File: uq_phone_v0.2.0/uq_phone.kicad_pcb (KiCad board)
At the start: 4 copper layers, 42.8 x 103.8 mm, 146 parts, among them J1 USB4105-GF-A, J10 SJ-3551B-MSMT-TR-67, J11 Conn_01x02, J2 BM03B-ACHSS-GAN-TF_LF__SN_, J3 20279-001E-03, J4 20279-001E-03, J5 6871XX14022_68715014022, J6 Conn_ARM_SWD_TagConnect_TC2030, J7 Conn_01x02, J8 KP15B-6S-SF_800_, M1 VCDM0834B004L, Q1 MMBT3904LP-7, Q2 MMBT3904LP-7, U1 MCP73871-2CCI_ML, U10 TPD3F303DQDR, U11 TPD8F003DQDR, U12 MCP1664T-E/OT, U13 TS3A5018RSVR, U14 NAU88C22YG, U2 TPS62162DSGR, U3 BQ27441DRZR-G1A, U4 WP SNAP-IN BASE_6000636, U5 TXB0108RGYR, U6 TXB0108RGYR, U7 STM32H733VGTx, U8 LSM6DSVTR, U9 DRV2603RUNR

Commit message: Clean repo
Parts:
- removed J1: USB4105-GF-A, USB_C_connector:GCT_USB4105-GF-A
- removed J10: SJ-3551B-MSMT-TR-67, SJ-3551B-MSMT-TR-67:CUI_SJ-3551B-MSMT-TR-67
- removed J11: Conn_01x02, Connector_Wire:SolderWire-0.25sqmm_1x02_P4.2mm_D0.65mm_OD1.7mm
- removed the J4 at (63.3, 83.3)
- removed the J5 at (31.0, 127.2)
- removed J7: Conn_01x02, Connector_Wire:SolderWire-0.1sqmm_1x02_P3.6mm_D0.4mm_OD1mm
- removed M1: VCDM0834B004L, custom_footprints:Motor_8mm
- removed R30, R31: 22R, Resistor_SMD:R_0402_1005Metric
- removed R34: 3.83R, Resistor_SMD:R_0603_1608Metric
- removed R35, R44, R49: 10k, Resistor_SMD:R_0402_1005Metric
- removed R37, R41, R43, R46, R47: 0R, Resistor_SMD:R_0603_1608Metric
- removed R4: 100k, Resistor_SMD:R_0402_1005Metric
- removed R45: 47k, Resistor_SMD:R_0402_1005Metric
- removed TP1: TestPoint, TestPoint:TestPoint_Pad_D1.5mm
- added J4: 20279-001E-03, 20279-001E-03:IPEX_20279-001E-03, F.Cu at (116.3, 24.4)
- added J4: 20279-001E-03, 20279-001E-03:IPEX_20279-001E-03, F.Cu at (114.3, 67.8)
- added J5: 20279-001E-03, 20279-001E-03:IPEX_20279-001E-03, F.Cu at (138.6, 37.2)
- added J5: 20279-001E-03, 20279-001E-03:IPEX_20279-001E-03, F.Cu at (142.3, 79.1)
- added LED1: XL-1010RGBC, custom_footprints:XL-1010RGBC-WS2812B, B.Cu at (62.0, 107.3)
- added LED10: XL-1010RGBC, custom_footprints:XL-1010RGBC-WS2812B, B.Cu at (64.6, 100.4)
- added LED11: XL-1010RGBC, custom_footprints:XL-1010RGBC-WS2812B, B.Cu at (64.6, 98.1)
- added LED12: XL-1010RGBC, custom_footprints:XL-1010RGBC-WS2812B, B.Cu at (64.6, 95.8)
- added LED13: XL-1010RGBC, custom_footprints:XL-1010RGBC-WS2812B, B.Cu at (67.2, 107.3)
- added LED14: XL-1010RGBC, custom_footprints:XL-1010RGBC-WS2812B, B.Cu at (67.2, 105.0)
- added LED15: XL-1010RGBC, custom_footprints:XL-1010RGBC-WS2812B, B.Cu at (67.2, 102.7)
- added LED16: XL-1010RGBC, custom_footprints:XL-1010RGBC-WS2812B, B.Cu at (67.2, 100.4)
- added LED17: XL-1010RGBC, custom_footprints:XL-1010RGBC-WS2812B, B.Cu at (67.2, 98.1)
- added LED2: XL-1010RGBC, custom_footprints:XL-1010RGBC-WS2812B, B.Cu at (62.0, 105.0)
- added LED3: XL-1010RGBC, custom_footprints:XL-1010RGBC-WS2812B, B.Cu at (62.0, 102.7)
- added LED4: XL-1010RGBC, custom_footprints:XL-1010RGBC-WS2812B, B.Cu at (62.0, 100.4)
- added LED5: XL-1010RGBC, custom_footprints:XL-1010RGBC-WS2812B, B.Cu at (62.0, 98.1)
- added LED6: XL-1010RGBC, custom_footprints:XL-1010RGBC-WS2812B, B.Cu at (62.0, 95.8)
- added LED7: XL-1010RGBC, custom_footprints:XL-1010RGBC-WS2812B, B.Cu at (64.6, 107.3)
- added LED8: XL-1010RGBC, custom_footprints:XL-1010RGBC-WS2812B, B.Cu at (64.6, 105.0)
- added LED9: XL-1010RGBC, custom_footprints:XL-1010RGBC-WS2812B, B.Cu at (64.6, 102.7)
- added R23: 10k, Resistor_SMD:R_0402_1005Metric, F.Cu at (60.5, 28.1)
- added REF**: HIROSE_KP15B-6S-SF_800_, KP15B-6S-SF_800_:HIROSE_KP15B-6S-SF_800_, F.Cu at (54.4, 51.0)
- added SW1: SKTAAAE010, custom_footprints:SKTAAAE010, B.Cu at (39.5, 107.0)
- added SW10: SKTAAAE010, custom_footprints:SKTAAAE010, B.Cu at (44.1, 107.0)
- added SW11: SKTAAAE010, custom_footprints:SKTAAAE010, B.Cu at (44.1, 103.8)
- added SW12: SKTAAAE010, custom_footprints:SKTAAAE010, B.Cu at (44.1, 100.8)
- added SW13: SKTAAAE010, custom_footprints:SKTAAAE010, B.Cu at (44.1, 97.7)
- added SW14: SKTAAAE010, custom_footprints:SKTAAAE010, B.Cu at (44.1, 94.5)
- added SW15: SKTAAAE010, custom_footprints:SKTAAAE010, B.Cu at (44.1, 91.5)
- added SW16: SKSCLCE010, custom_footprints:SKSCLCE010, B.Cu at (79.3, 41.0)
- added SW17: SKTAAAE010, custom_footprints:SKTAAAE010, B.Cu at (44.1, 88.3)
- added SW18: SKTAAAE010, custom_footprints:SKTAAAE010, B.Cu at (44.1, 85.2)
- added SW19: SKTAAAE010, custom_footprints:SKTAAAE010, B.Cu at (48.9, 107.0)
- added SW2: SKTAAAE010, custom_footprints:SKTAAAE010, B.Cu at (39.5, 103.8)
- added SW20: SKTAAAE010, custom_footprints:SKTAAAE010, B.Cu at (48.9, 103.8)
- added SW21: SKTAAAE010, custom_footprints:SKTAAAE010, B.Cu at (48.9, 100.8)
- added SW22: SKSCLCE010, custom_footprints:SKSCLCE010, B.Cu at (84.0, 41.0)
- added SW23: SKTAAAE010, custom_footprints:SKTAAAE010, B.Cu at (48.9, 97.7)
- added SW24: SKTAAAE010, custom_footprints:SKTAAAE010, B.Cu at (48.9, 94.5)
- added SW25: SKTAAAE010, custom_footprints:SKTAAAE010, B.Cu at (48.9, 91.5)
- added SW26: SKTAAAE010, custom_footprints:SKTAAAE010, B.Cu at (48.9, 88.3)
- added SW27: SKTAAAE010, custom_footprints:SKTAAAE010, B.Cu at (48.9, 85.2)
- added SW28: SKTAAAE010, custom_footprints:SKTAAAE010, B.Cu at (53.5, 107.0)
- added SW29: SKTAAAE010, custom_footprints:SKTAAAE010, B.Cu at (53.5, 103.8)
- added SW3: SKTAAAE010, custom_footprints:SKTAAAE010, B.Cu at (39.5, 100.8)
- added SW30: SKTAAAE010, custom_footprints:SKTAAAE010, B.Cu at (53.5, 100.8)
- added SW31: SKTAAAE010, custom_footprints:SKTAAAE010, B.Cu at (53.5, 97.7)
- added SW32: SKTAAAE010, custom_footprints:SKTAAAE010, B.Cu at (53.5, 94.5)
- added SW33: SKTAAAE010, custom_footprints:SKTAAAE010, B.Cu at (53.5, 91.5)
- added SW34: SKTAAAE010, custom_footprints:SKTAAAE010, B.Cu at (53.5, 88.3)
- added SW35: SKTAAAE010, custom_footprints:SKTAAAE010, B.Cu at (53.5, 85.2)
- added SW36: SKTAAAE010, custom_footprints:SKTAAAE010, B.Cu at (58.2, 107.0)
- added SW37: SKTAAAE010, custom_footprints:SKTAAAE010, B.Cu at (58.2, 103.8)
- added SW38: SKTAAAE010, custom_footprints:SKTAAAE010, B.Cu at (58.2, 100.8)
- added SW39: SKTAAAE010, custom_footprints:SKTAAAE010, B.Cu at (58.2, 97.7)
- added SW4: SKTAAAE010, custom_footprints:SKTAAAE010, B.Cu at (39.5, 97.7)
- added SW40: SKTAAAE010, custom_footprints:SKTAAAE010, B.Cu at (58.2, 94.5)
- added SW41: SKTAAAE010, custom_footprints:SKTAAAE010, B.Cu at (58.2, 91.5)
- added SW5: SKTAAAE010, custom_footprints:SKTAAAE010, B.Cu at (39.5, 94.5)
- added SW6: SKSCLCE010, custom_footprints:SKSCLCE010, B.Cu at (78.7, 34.1)
- added SW7: SKTAAAE010, custom_footprints:SKTAAAE010, B.Cu at (39.5, 91.5)
- added SW8: SKTAAAE010, custom_footprints:SKTAAAE010, B.Cu at (39.5, 88.3)
- added SW9: SKTAAAE010, custom_footprints:SKTAAAE010, B.Cu at (39.5, 85.2)
- C1, C15, C16, C17, C18, C5, C6, L1, MK1, R11, U3: moved to B.Cu
- C14: value 100nF -> 4.7uF; moved to B.Cu
- C19: value 4.7uF -> 100nF; moved to B.Cu
- C2: value 4.7uF -> 22uF; footprint Capacitor_SMD:C_0402_1005Metric -> Capacitor_SMD:C_0603_1608Metric; moved to B.Cu
- C20: value 2.2uF -> 100nF; moved to B.Cu
- C21: value 2.2uF -> 100nF
- C25, C26: value 100nF -> 2.2uF
- C27: value 100nF -> 10uF; footprint Capacitor_SMD:C_0402_1005Metric -> Capacitor_SMD:C_0603_1608Metric
- C28, C36: value 100nF -> 4.7uF
- C3: value 4.7uF -> 10uF; footprint Capacitor_SMD:C_0402_1005Metric -> Capacitor_SMD:C_0603_1608Metric; moved to B.Cu
- C34: value 10uF -> 100nF; footprint Capacitor_SMD:C_0603_1608Metric -> Capacitor_SMD:C_0402_1005Metric
- C35: value 4.7uF -> 100nF
- C38: value 1uF -> 100nF
- C39, C41, C43: value 1uF -> 4.7uF
- C4: value 10uF -> 4.7uF; footprint Capacitor_SMD:C_0603_1608Metric -> Capacitor_SMD:C_0402_1005Metric; moved to B.Cu
- C40: value 33pF -> 4.7uF
- C45, C47, C48, C49: value 4.7uF -> 1uF
- C46: value 4.7uF -> 33pF
- C7: value 22uF -> 4.7uF; footprint Capacitor_SMD:C_0603_1608Metric -> Capacitor_SMD:C_0402_1005Metric; moved to B.Cu
- J2: value BM03B-ACHSS-GAN-TF_LF__SN_ -> 124018312112A; footprint BM03B-ACHSS-GAN-TF_LF__SN_:JST_BM03B-ACHSS-GAN-TF_LF__SN_ -> 124018312112A:AMPHENOL_124018312112A
- J3: value 20279-001E-03 -> BM03B-ACHSS-GAN-TF_LF__SN_; footprint 20279-001E-03:IPEX_20279-001E-03 -> BM03B-ACHSS-GAN-TF_LF__SN_:JST_BM03B-ACHSS-GAN-TF_LF__SN_
- J8: value KP15B-6S-SF_800_ -> MCS-302S-C1; footprint KP15B-6S-SF_800_:HIROSE_KP15B-6S-SF_800_ -> custom_footprints:SIM-SMD_MCS-302S-C1
- R1: value 270k -> 100k; moved to B.Cu
- R10: value 0R -> 2.2k; footprint Resistor_SMD:R_0805_2012Metric -> Resistor_SMD:R_0402_1005Metric; moved to B.Cu
- R12: value 4.7k -> 0R
- R13: value 47k -> 0R
- R14, R15: footprint Resistor_SMD:R_0603_1608Metric -> Resistor_SMD:R_0402_1005Metric
- R16, R21, R22: value 0R -> 4.7k; footprint Resistor_SMD:R_0603_1608Metric -> Resistor_SMD:R_0402_1005Metric
- R19: value 0R -> 47k; footprint Resistor_SMD:R_0603_1608Metric -> Resistor_SMD:R_0402_1005Metric
- R2: value 100k -> 5.1k
- R20, R40: value 0R -> 10k; footprint Resistor_SMD:R_0603_1608Metric -> Resistor_SMD:R_0402_1005Metric
- R24, R25: value 4.7k -> 10k
- R26, R27: value 10k -> 22R
- R28: value 0R -> 22R; footprint Resistor_SMD:R_0603_1608Metric -> Resistor_SMD:R_0402_1005Metric
- R29: value 0R -> 3.83R
- R3: value 2.2k -> 5.1k
- R32: value 22R -> 10k
- R36: value 10k -> 2.2k
- R38: value 2.2k -> 47k
- R42: value 0R -> 330R; footprint Resistor_SMD:R_0603_1608Metric -> Resistor_SMD:R_0402_1005Metric; moved to B.Cu
- R5: value 5.1k -> 270k; moved to B.Cu
- R7: value 10k -> 100k; moved to B.Cu
- R8: value 10m -> 10k; footprint Resistor_SMD:R_0805_2012Metric -> Resistor_SMD:R_0402_1005Metric; moved to B.Cu
- R9: value 5.1k -> 10m; footprint Resistor_SMD:R_0402_1005Metric -> Resistor_SMD:R_0805_2012Metric; moved to B.Cu
- TP2, TP3, TP4, TP5, TP6, TP7: moved to F.Cu
- U1: value MCP73871-2CCI_ML -> TPS62162DSGR; footprint MCP73871-2CCI_ML:QFN50P400X400X100-21N -> TPS62162DSGR:SON50P200X200X80-9N; moved to B.Cu
- U10: value TPD3F303DQDR -> TPD8F003DQDR; footprint TPD3F303DQDR:SON40P170X135X80-9N -> TPD8F003DQDR:SON40P135X330X80-17N
- U11: value TPD8F003DQDR -> LSM6DSVTR; footprint TPD8F003DQDR:SON40P135X330X80-17N -> LSM6DSVTR:LGA14-L_2P59X3P1X0P5_STM
- U12: value MCP1664T-E/OT -> DRV2603RUNR; footprint MCP1664T_E_OT:SOT-23-5_OT_MCH -> DRV2603RUNR:QFN50P200X200X80-10N; moved to B.Cu
- U2: value TPS62162DSGR -> MCP73871-2CCI_ML; footprint TPS62162DSGR:SON50P200X200X80-9N -> MCP73871-2CCI_ML:QFN50P400X400X100-21N; moved to B.Cu
- U4: footprint WP_SNAP-IN_BASE:SIERRA_WP_SNAP-IN_BASE -> RC7620_1104625:XCVR_RC7620_1104625
- U6: value TXB0108RGYR -> STM32H733VGHx; footprint TXB0108RGYR:IC_TXB0108RGYR -> Package_BGA:TFBGA-100_8x8mm_Layout10x10_P0.8mm
- U7: value STM32H733VGTx -> TXB0108RGYR; footprint Package_QFP:LQFP-100_14x14mm_P0.5mm -> TXB0108RGYR:IC_TXB0108RGYR
- U8: value LSM6DSVTR -> TPD3F303DQDR; footprint LSM6DSVTR:LGA14-L_2P59X3P1X0P5_STM -> TPD3F303DQDR:SON40P170X135X80-9N
- U9: value DRV2603RUNR -> MCP1664T-E/OT; footprint DRV2603RUNR:QFN50P200X200X80-10N -> MCP1664T_E_OT:SOT-23-5_OT_MCH
- moved R6 138.0 mm to (64.0, 25.0), turned to 180 degrees
- moved C34 126.0 mm to (68.3, 21.9), turned to -90 degrees
- moved R25 126.0 mm to (59.5, 20.2), turned to 0 degrees
- moved C35 125.5 mm to (65.4, 22.6), turned to 0 degrees
- moved R24 117.0 mm to (60.5, 29.1), turned to 180 degrees
- moved C39 116.6 mm to (142.2, 86.0), turned to 0 degrees
- moved C19 116.2 mm to (68.2, 28.9)
- moved C25 115.0 mm to (60.6, 31.1), turned to 180 degrees
- moved R27 114.7 mm to (49.2, 38.7), turned to 0 degrees
- moved R28 113.8 mm to (49.2, 39.6)
- moved C26 112.7 mm to (60.6, 30.2), turned to 180 degrees
- moved R26 112.7 mm to (49.2, 40.6), turned to 0 degrees
- moved U9 108.2 mm to (36.8, 44.0)
- moved R29 107.8 mm to (33.7, 46.2), turned to 0 degrees
- moved L2 107.7 mm to (36.8, 40.1)
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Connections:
- C1 pad 1: VUSB -> GND
- C1 pad 2: GND -> MCP_OUT
- C10 pad 1: +VMOB -> VBAT
- C11 pad 1: +VMOB -> VBAT
- C12 pad 1: +VMOB -> VBAT
- C13 pad 1: +VMOB -> VBAT
- C14 pad 1: +1.8V -> +3.3V
- C15 pad 1: +1.8V -> GND
- C15 pad 2: GND -> +3.3V
- C16 pad 1: +3.3V -> GND
- C16 pad 2: GND -> +3.3V
- C17 pad 1: +3.3V -> GND
- C17 pad 2: GND -> +3.3V
- C18 pad 2: RST -> +3.3V
- C19 pad 1: +3.3V -> GND
- C19 pad 2: GND -> +3.3V
- C2 pad 1: VBAT -> +3.3V
- C20 pad 1: Net-(C20-Pad1) -> GND
- C20 pad 2: GND -> RST
- C21 pad 1: Net-(C21-Pad1) -> +1.8V
- C22 pad 1: GND -> +3.3V
- C22 pad 2: +3.3V -> GND
- C23 pad 1: GND -> +1.8V
- C23 pad 2: +3.3V -> GND
- C24 pad 1: GND -> +3.3V
- C24 pad 2: +3.3V -> GND
- C25 pad 1: GND -> Net-(C25-Pad1)
- C25 pad 2: +3.3V -> GND
- C26 pad 1: GND -> Net-(C26-Pad1)
- C26 pad 2: +3.3V -> GND
- C28 pad 1: +3.3V -> DISP_LEDA
- C3 pad 1: MCP_OUT -> VUSB
- C35 pad 1: DISP_LEDA -> +3.3V
- C36 pad 1: +1.8V -> Net-(MK1-OUTPUT)
- C36 pad 2: GND -> MIC_OUT
- C37 pad 1: HP_MIC -> AGND
- C37 pad 2: Net-(C37-Pad2) -> MIC_GND
- C38 pad 1: HP_LEFT -> +1.8V
- C38 pad 2: Net-(C38-Pad2) -> GND
- C39 pad 1: HP_RIGHT -> Net-(U14-VDDA)
- C39 pad 2: Net-(C39-Pad2) -> AGND
- C4 pad 1: GND -> MCP_OUT
- C4 pad 2: MCP_OUT -> GND
- C40 pad 1: Net-(U14-MCLK) -> Net-(U14-VDDA)
- C40 pad 2: GND -> AGND
- C41 pad 1: Net-(U14-RMICN) -> +1.8V
- C41 pad 2: AGND -> GND
- C42 pad 1: Net-(MK1-OUTPUT) -> +1.8V
- C42 pad 2: MIC_OUT -> GND
- C43 pad 1: AGND -> Net-(U14-VREF)
- C43 pad 2: MIC_GND -> AGND
- C44 pad 1: Net-(U14-VDDB) -> MIC_BIAS
- C44 pad 2: GND -> AGND
- C45 pad 1: MIC_BIAS -> Net-(U14-RMICN)
- C46 pad 1: Net-(U14-VDDB) -> MOB_SYS_CLK
- C47 pad 1: Net-(U14-VDDA) -> Net-(U14-RMICP)
- C47 pad 2: AGND -> HP_MIC
- C48 pad 1: Net-(U14-VREF) -> HP_LEFT
- C48 pad 2: AGND -> Net-(C48-Pad2)
- C49 pad 1: Net-(U14-VDDA) -> HP_RIGHT
- C49 pad 2: AGND -> Net-(C49-Pad2)
- C7 pad 1: +3.3V -> VBAT
- C8 pad 1: +VMOB -> VBAT
- C9 pad 1: +VMOB -> VBAT
- FB1 pad 1: GND -> Net-(U14-VDDA)
- FB1 pad 2: AGND -> +3.3V
- FB2 pad 1: Net-(U14-VDDA) -> GND
- FB2 pad 2: +3.3V -> AGND
- J3 pad 1: MOB_MAIN_ANT -> GND
- J3 pad 2: GND -> BAT_THERM
- J3 pad 3: (no net) -> Net-(U3-BAT)
- L1 pad 1: Net-(U2-SW) -> Net-(U1-SW)
- R1 pad 1: Net-(U1-VPCC) -> Net-(U1-PG)
- R1 pad 2: VUSB -> +3.3V
- R10 pad 1: +VMOB -> Net-(U2-PROG1)
- R10 pad 2: VBAT -> GND
- R11 pad 1: Net-(U2-PG) -> GND
- R11 pad 2: +3.3V -> Net-(U2-PROG3)
- R12 pad 1: Net-(Q1-Pad1) -> Net-(U4A-UART1_TX)
- R12 pad 2: MOB_PWR_CTL -> MOB_TXD
- R13 pad 1: GND -> Net-(U4A-UART1_RTS)
- R13 pad 2: Net-(Q1-Pad1) -> MOB_RTS
- R14 pad 1: /Mobile/MOB_USB_N -> Net-(U4A-UART1_RX)
- R14 pad 2: USB_N -> MOB_RXD
- R15 pad 1: /Mobile/MOB_USB_P -> Net-(U4A-UART1_CTS)
- R15 pad 2: USB_P -> MOB_CTS
- R16 pad 1: Net-(U4A-USB_VBUS) -> Net-(Q1-Pad1)
- R16 pad 2: VUSB -> MOB_PWR_CTL
- R18 pad 2: Net-(Q2-Pad1) -> Net-(Q1-Pad1)
- R19 pad 1: Net-(U4A-UART1_TX) -> GND
- R19 pad 2: MOB_TXD -> Net-(Q2-Pad1)
- R2 pad 2: Net-(U1-VPCC) -> Net-(J2-CC1)
- R20 pad 1: Net-(U4A-UART1_RTS) -> GND
- R20 pad 2: MOB_RTS -> Net-(U6-BOOT0)
- R21 pad 1: Net-(U4A-UART1_RX) -> SCL
- R21 pad 2: MOB_RXD -> +3.3V
- R22 pad 1: Net-(U4A-UART1_CTS) -> SDA
- R22 pad 2: MOB_CTS -> +3.3V
- R24 pad 1: SCL -> MCP_STAT1
- R25 pad 1: SDA -> uSD_DET
- R26 pad 1: MCP_STAT2 -> Net-(U8-DATA2_IN)
- R26 pad 2: +3.3V -> SIM_DATA
- R27 pad 1: MCP_STAT1 -> Net-(U8-DATA1_IN)
- R27 pad 2: +3.3V -> SIM_RST
- R28 pad 1: Net-(U9-LRA/~{ERM}) -> Net-(U8-CLK_IN)
- R28 pad 2: +3.3V -> SIM_CLK
- R29 pad 2: Net-(U9-LRA/~{ERM}) -> DISP_LEDK
- R3 pad 1: Net-(U1-PROG1) -> GND
- R3 pad 2: GND -> Net-(J2-CC2)
- R32 pad 1: Net-(U10-CLK_IN) -> AUD_SW_L
- R32 pad 2: SIM_CLK -> +1.8V
- R33 pad 1: uSD_DET -> GND
- R33 pad 2: +3.3V -> Net-(U13-~{EN})
- R36 pad 1: GND -> HP_MIC
- R36 pad 2: Net-(U13-~{EN}) -> MIC_BIAS
- R38 pad 1: Net-(C37-Pad2) -> HP_DET
- R38 pad 2: MIC_BIAS -> +1.8V
- R39 pad 1: Net-(C38-Pad2) -> Net-(C48-Pad2)
- R40 pad 1: MOB_AUD_SYNC -> Net-(C49-Pad2)
- R40 pad 2: AUD_SYNC -> AGND
- R42 pad 1: MOB_AUD_IN -> Net-(LED15-DI)
- R42 pad 2: AUD_IN -> LED_DATA
- R5 pad 1: GND -> Net-(U2-VPCC)
- R5 pad 2: Net-(J1-CC2) -> VUSB
- R6 pad 1: GND -> FUEL_GPO
- R6 pad 2: Net-(J1-CC1) -> +3.3V
- R7 pad 2: Net-(U3-BIN) -> Net-(U2-VPCC)
- R8 pad 1: Net-(U3-BAT) -> GND
- R8 pad 2: VBAT -> Net-(U3-BIN)
- R9 pad 1: FUEL_GPO -> Net-(U3-BAT)
- R9 pad 2: +3.3V -> VBAT
- TP2 pad 1: GND -> VUSB
- TP4 pad 1: AGND -> VBAT
- TP5 pad 1: VBAT -> +1.8V
- TP6 pad 1: +VMOB -> GND
- TP7 pad 1: +1.8V -> AGND
- TP8 pad 1: Net-(U4A-TP1_BOOTPIN) -> Net-(U4A-TX_ON)
- TP9 pad 1: Net-(U4A-TX_ON) -> Net-(U4A-TP1_BOOTPIN)
- U1 pad 1: MCP_OUT -> GND
- U1 pad 2: Net-(U1-VPCC) -> MCP_OUT
- U1 pad 3: VUSB -> MCP_OUT
- U1 pad 4: VUSB -> GND
- U1 pad 5: BAT_THERM -> GND
- U1 pad 6: MCP_PG -> +3.3V
- U1 pad 7: MCP_STAT2 -> Net-(U1-SW)
- U1 pad 8: MCP_STAT1 -> Net-(U1-PG)
- U1 pad 9: VUSB -> GND
- U10 pad 1: Net-(J8B-RST) -> uSD_DAT2
- U10 pad 2: Net-(J8B-CLK_2) -> uSD_DAT3
- U10 pad 3: Net-(J8B-I/O) -> uSD_CMD
- U10 pad 4: (no net) -> uSD_CLK
- U10 pad 5: SIM_VDD -> uSD_DET
- U10 pad 6: Net-(U10-DATA2_IN) -> uSD_DAT0
- U10 pad 7: Net-(U10-CLK_IN) -> uSD_DAT1
- U10 pad 8: Net-(U10-DATA1_IN) -> unconnected-(U10-CH8_IN-Pad8)
- U10 pad 9: GND -> unconnected-(U10-CH8_OUT-Pad9)
- U11 pad 1: uSD_DAT2 -> GND
- U11 pad 10: Net-(J8A-DAT1) -> unconnected-(U11-OCS_AUX-Pad10)
- U11 pad 11: Net-(J8A-DAT0) -> unconnected-(U11-SDO_AUX-Pad11)
- U11 pad 12: Net-(U11-CH5_OUT) -> +3.3V
- U11 pad 13: Net-(J8A-CLK) -> SCL
- U11 pad 14: Net-(J8A-CMD) -> SDA
- U11 pad 2: uSD_DAT3 -> GND
- U11 pad 3: uSD_CMD -> GND
- U11 pad 4: uSD_CLK -> unconnected-(U11-INT1-Pad4)
- U11 pad 5: uSD_DET -> +3.3V
- U11 pad 6: uSD_DAT0 -> GND
- U11 pad 7: uSD_DAT1 -> GND
- U11 pad 8: unconnected-(U11-CH8_IN-Pad8) -> +3.3V
- U12 pad 1: Net-(D2-A) -> VIB_EN
- U12 pad 2: GND -> VIB_PWM
- U12 pad 3: DISP_LEDK -> GND
- U12 pad 4: DISP_BL -> (no net)
- U12 pad 5: +3.3V -> GND
- U14 pad 11: Net-(U14-MCLK) -> MOB_SYS_CLK
- U14 pad 13: Net-(U14-VDDB) -> +1.8V
- U14 pad 14: Net-(U14-VDDB) -> +1.8V
- U14 pad 4: HP_MIC -> Net-(U14-RMICP)
- U2 pad 1: GND -> MCP_OUT
- U2 pad 2: MCP_OUT -> Net-(U2-VPCC)
- U2 pad 3: MCP_OUT -> VUSB
- U2 pad 4: GND -> VUSB
- U2 pad 5: GND -> BAT_THERM
- U2 pad 6: +3.3V -> MCP_PG
- U2 pad 7: Net-(U2-SW) -> MCP_STAT2
- U2 pad 8: Net-(U2-PG) -> MCP_STAT1
- U2 pad 9: GND -> VUSB
- U4 pad 12: /Mobile/MOB_USB_N -> unconnected-(U4A-USB_D--Pad12)
- U4 pad 13: /Mobile/MOB_USB_P -> unconnected-(U4A-USB_D+-Pad13)
- U4 pad 157: +VMOB -> VBAT
- U4 pad 158: +VMOB -> VBAT
- U4 pad 16: Net-(U4A-USB_VBUS) -> unconnected-(U4A-USB_VBUS-Pad16)
- U4 pad 61: +VMOB -> VBAT
- U4 pad 62: +VMOB -> VBAT
- U4 pad 63: +VMOB -> VBAT
- U7 pad 1: PB_HASH -> AUD_SDA
- U7 pad 10: GND -> +1.8V
- U7 pad 11: +3.3V -> GND
- U7 pad 12: PB_8 -> MCU_AUD_OUT_L_H
- U7 pad 13: PB_9 -> MCU_AUD_BCLK_H
- U7 pad 14: RST -> AUD_SW_H
- U7 pad 15: PB_MENU_L -> MCU_AUD_SYNC_H
- U7 pad 16: PB_MENU_R -> HP_DET_MCU
- U7 pad 17: unconnected-(U7-PC2_C-Pad17) -> MOB_WAKE_H
- U7 pad 18: unconnected-(U7-PC3_C-Pad18) -> SCL
- U7 pad 19: GND -> +3.3V
- U7 pad 2: PB_1 -> +1.8V
- U7 pad 20: unconnected-(U7-VREF+-Pad20) -> SDA
- U7 pad 21: unconnected-(U7-VDDA-Pad21) -> GND
- U7 pad 3: PB_2 -> AUD_SCL
- U7 pad 4: PB_3 -> MOB_WAKE_L
- U7 pad 5: PB_4 -> HP_DET
- U7 pad 6: unconnected-(U7-VBAT-Pad6) -> MCU_AUD_SYNC_L
- U7 pad 7: PB_5 -> AUD_SW_L
- U7 pad 8: PB_6 -> MCU_AUD_BCLK_L
- U7 pad 9: PB_7 -> MCU_AUD_OUT_L
- U8 pad 1: GND -> Net-(J8B-SIM_1_RST)
- U8 pad 2: GND -> Net-(J8B-SIM_1_CLK)
- U8 pad 3: GND -> Net-(J8B-SIM_1_DATA)
- U8 pad 4: unconnected-(U8-INT1-Pad4) -> (no net)
- U8 pad 5: +3.3V -> SIM_VDD
- U8 pad 6: GND -> Net-(U8-DATA2_IN)
- U8 pad 7: GND -> Net-(U8-CLK_IN)
- U8 pad 8: +3.3V -> Net-(U8-DATA1_IN)
- U8 pad 9: unconnected-(U8-INT2-Pad9) -> GND
- U9 pad 1: VIB_EN -> Net-(D2-A)
- U9 pad 2: VIB_PWM -> GND
- U9 pad 3: Net-(U9-LRA/~{ERM}) -> DISP_LEDK
- U9 pad 4: (no net) -> DISP_BL
- U9 pad 5: GND -> +3.3V
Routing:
- net +3.3V: track 246.4 -> 0.00 mm, vias 16 -> 0
- net +1.8V: track 115.8 -> 0.00 mm, vias 6 -> 0
- net AGND: track 111.9 -> 0.00 mm, vias 5 -> 0
- net Net-(MK1-OUTPUT): track 109.6 -> 0.00 mm, vias 2 -> 0
- net MIC_BIAS: track 106.3 -> 0.00 mm, vias 3 -> 0
- net SDA: track 91.7 -> 0.00 mm, vias 6 -> 0
- net SCL: track 91.6 -> 0.00 mm, vias 6 -> 0
- net HP_DET: track 89.6 -> 0.00 mm, vias 5 -> 0
- net +VMOB: track 81.8 -> 0.00 mm, vias 3 -> 0
- net GND: track 81.8 -> 0.00 mm, vias 375 -> 148
- net Net-(C37-Pad2): track 81.7 -> 0.00 mm, vias 2 -> 0
- net HP_RIGHT: track 78.2 -> 0.00 mm, vias 2 -> 0
- net HP_LEFT: track 75.5 -> 0.00 mm, vias 2 -> 0
- net Net-(U4A-USB_VBUS): track 63.0 -> 0.00 mm, vias 2 -> 0
- net /Mobile/MOB_USB_N: track 63.0 -> 0.00 mm, vias 2 -> 0
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- added copper zone on In3.Cu, net GND
- added copper zone on In4.Cu, net GND
- removed copper zone on F.Cu, net +VMOB
- removed copper zone on B.Cu, net AGND
- removed copper zone on F.Cu, net AGND
- removed copper zone on F.Cu, net MCP_OUT
- removed copper zone on F.Cu, net Net-(U2-SW)
- removed copper zone on F.Cu, net Net-(U3-BAT)
- removed copper zone on F.Cu, net VBAT
- removed copper zone on F.Cu, net VUSB
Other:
- board size 42.8 x 103.8 mm -> 118.2 x 108 mm
- copper layers 4 -> 6
- board text added: "Battery"
- board text added: "Non Socket Version"
- board text added: "Socket Version"
- board text added: "THIS IS A BACK VIEW R L"
- board text removed: "LEFT"
- board text removed: "RIGHT"

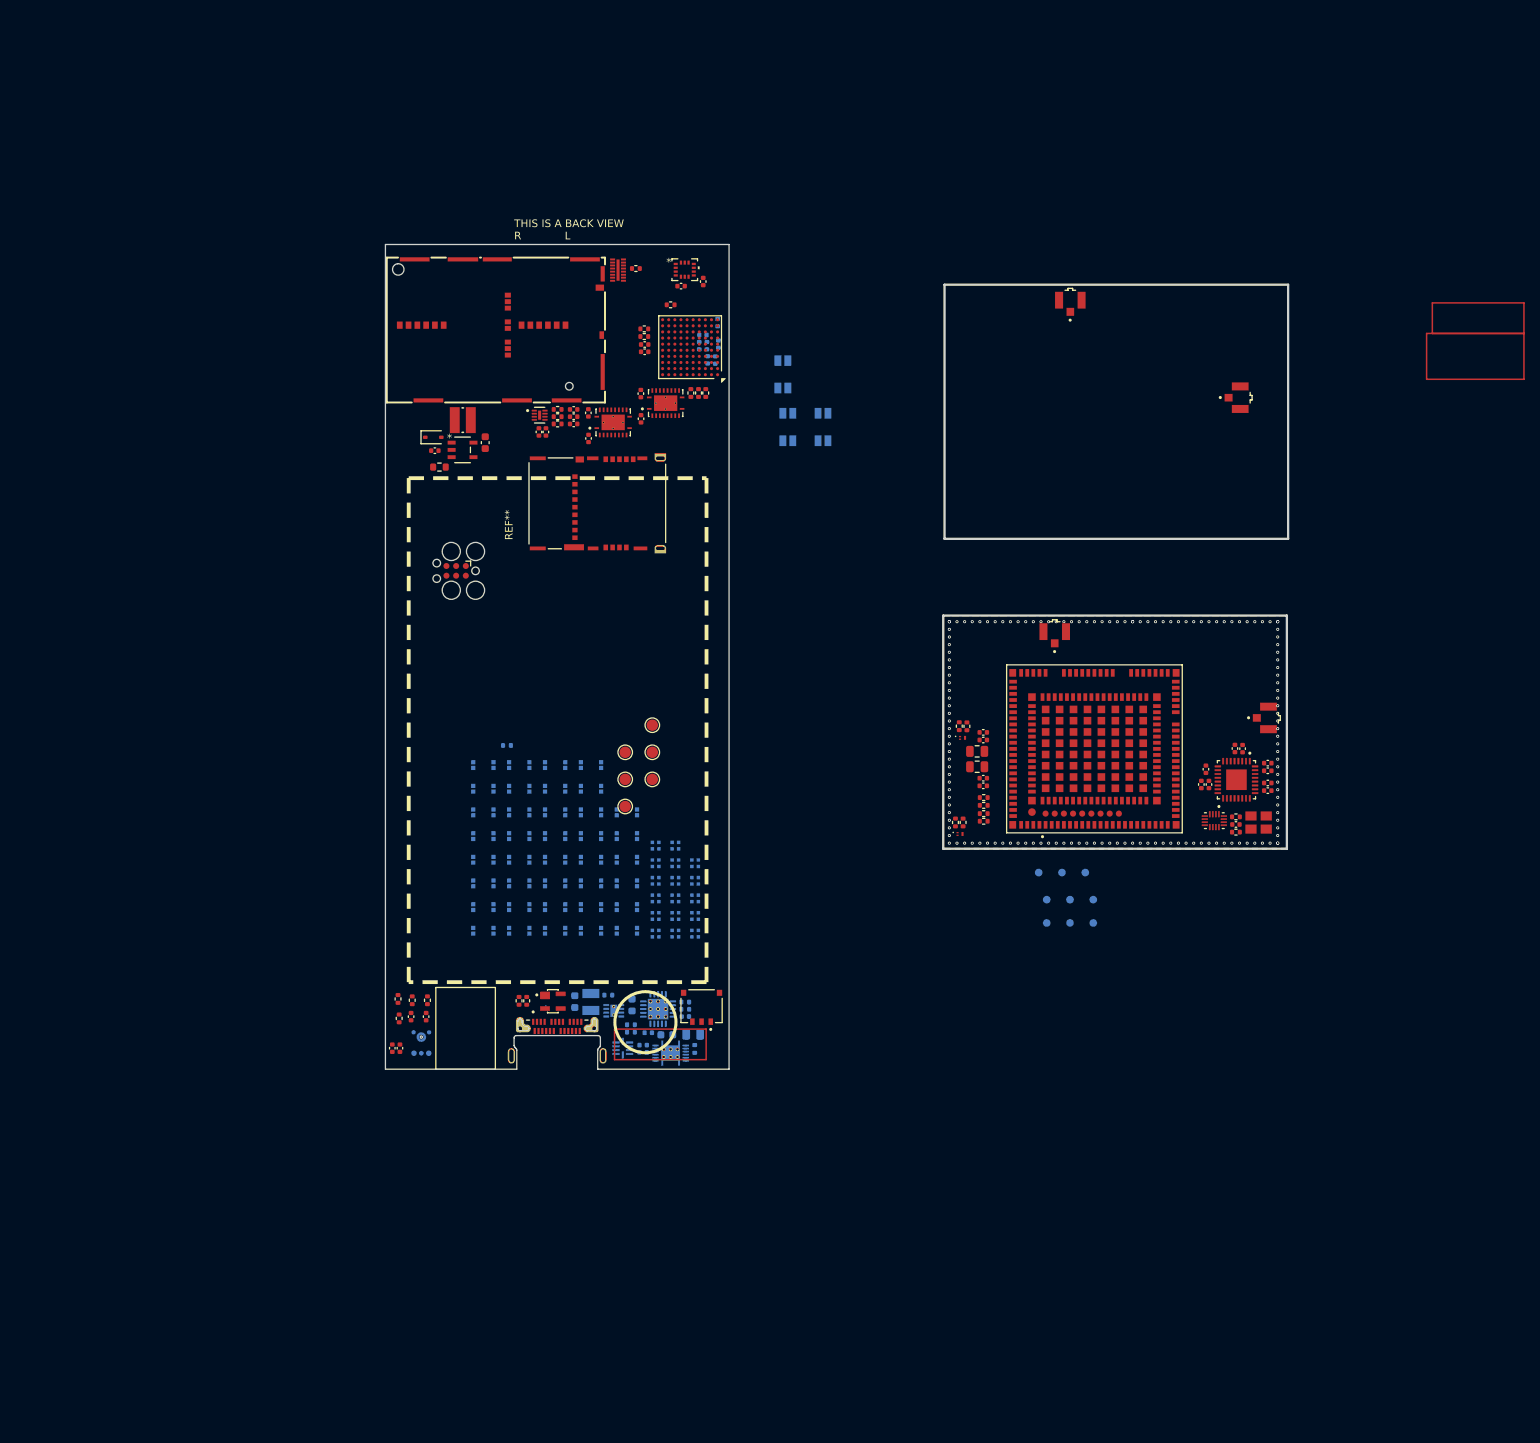
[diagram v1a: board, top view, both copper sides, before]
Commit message: Add more footprints, reduce sizes
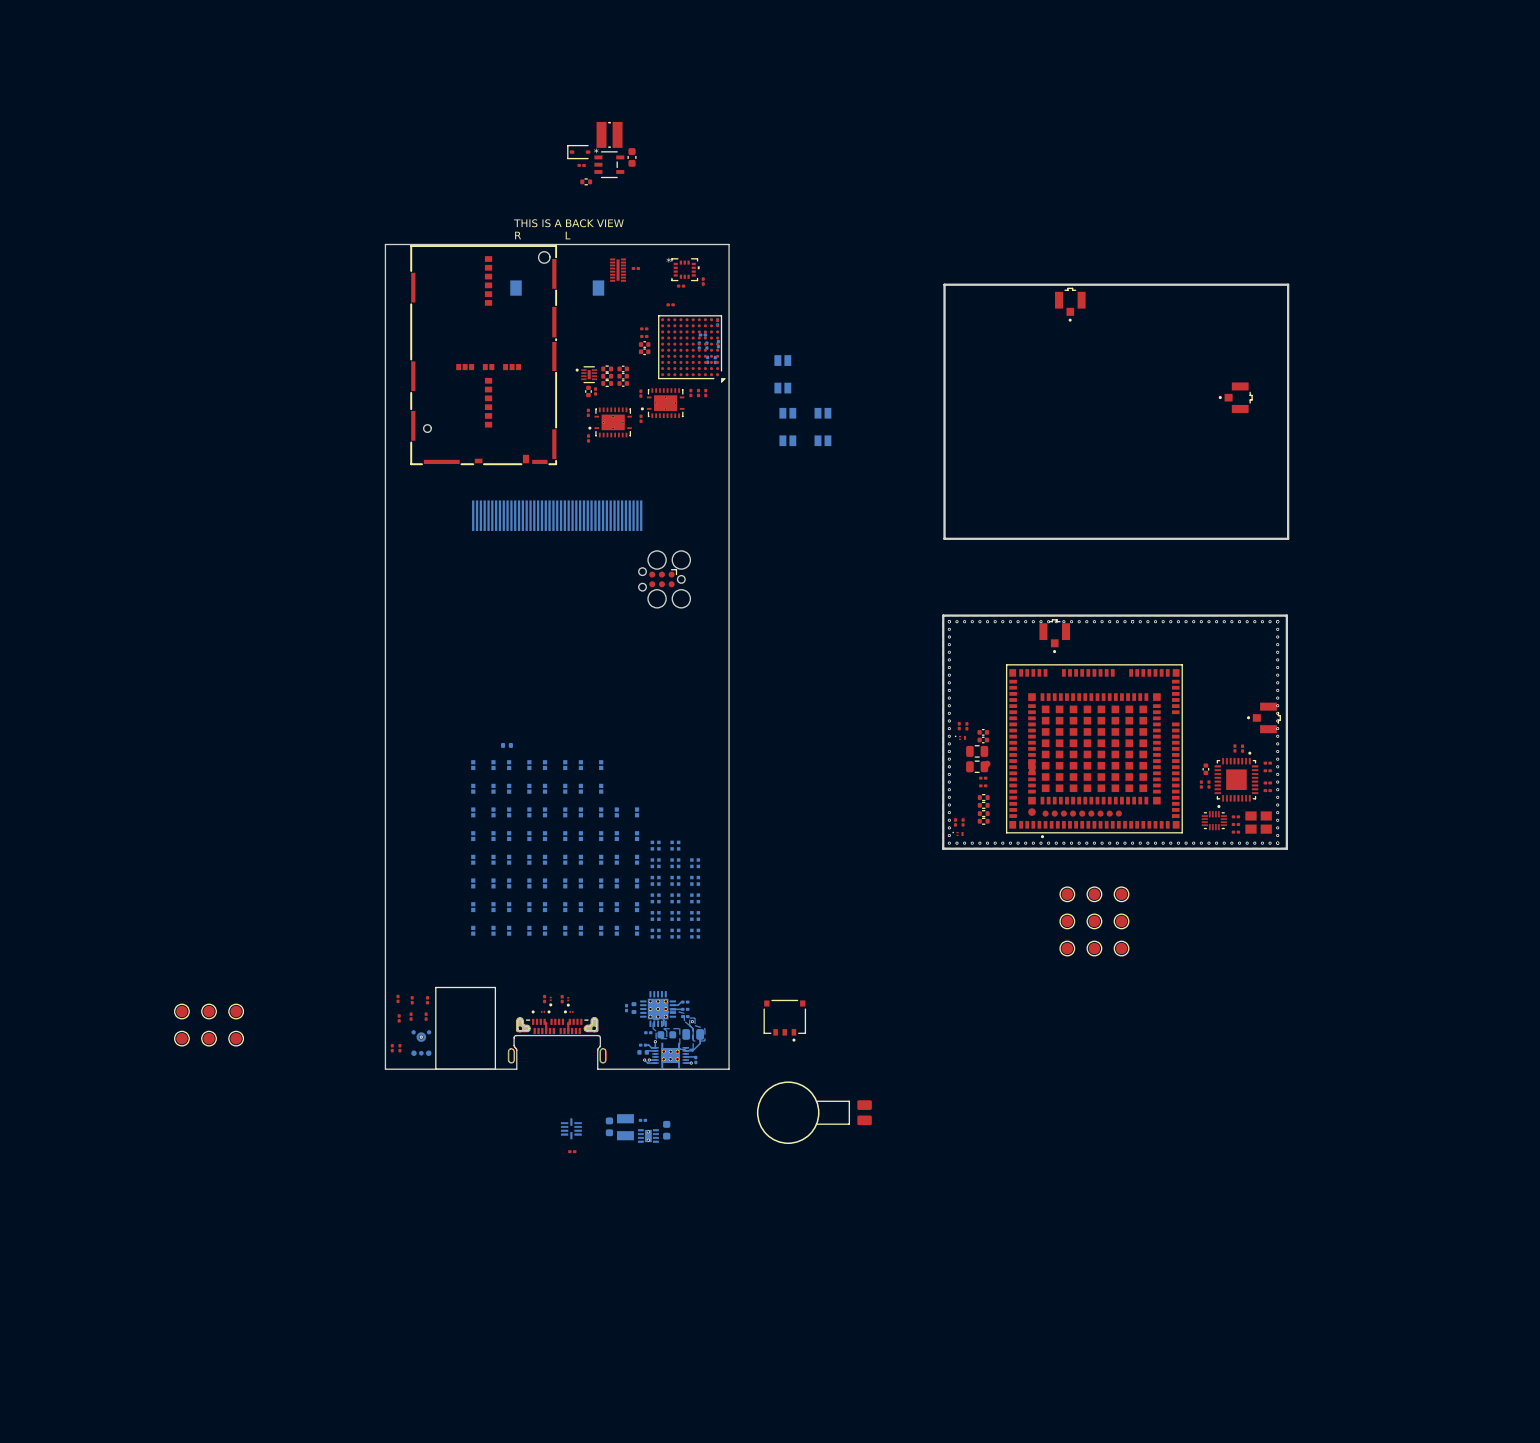
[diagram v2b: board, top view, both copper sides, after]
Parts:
- removed D1: SP0503BAHTG, SP0503BAHTG:SOT143
- removed REF**: HIROSE_KP15B-6S-SF_800_, KP15B-6S-SF_800_:HIROSE_KP15B-6S-SF_800_
- removed TP7: TestPoint, TestPoint:TestPoint_Pad_D1.5mm
- added C29: 100nF, Capacitor_SMD:C_0201_0603Metric, F.Cu at (51.1, 135.9)
- added D4: ESD441DPYR, ESD441DPLR:DIODFN60X30X32-2N, F.Cu at (47.3, 117.6)
- added D5: ESD441DPYR, ESD441DPLR:DIODFN60X30X32-2N, F.Cu at (51.0, 117.6)
- added D6: ESD441DPYR, ESD441DPLR:DIODFN60X30X32-2N, F.Cu at (50.6, 115.9)
- added D7: ESD441DPYR, ESD441DPLR:DIODFN60X30X32-2N, F.Cu at (48.3, 115.9)
- added Disp1: AFR240320A0-2.0INTM, custom_footprints:Display, B.Cu at (49.1, 50.7)
- added M1: C08-00A, custom_footprints:Motor_8mm, F.Cu at (79.4, 130.8)
- added SP1: MCABS-258-RC, custom_footprints:MCABS-258-RC, B.Cu at (49.1, 20.5)
- added TP1: TestPoint, TestPoint:TestPoint_Pad_D1.5mm, F.Cu at (0.00, 117.5)
- C10, C11, C14, C15, C16, C17, C18, C19, C20, C21, C22, C23, C24, C28, C32, C34, C35, C36, C37, C38, C39, C4, C40, C41, C42, C43, C44, C45, C47, C48, C49, C6, C7: footprint Capacitor_SMD:C_0402_1005Metric -> Capacitor_SMD:C_0201_0603Metric
- R1, R10, R11, R16, R17, R18, R19, R2, R20, R21, R22, R23, R24, R25, R3, R32, R33, R36, R38, R39, R40, R6, R7, R8: footprint Resistor_SMD:R_0402_1005Metric -> Resistor_SMD:R_0201_0603Metric
- R29: footprint Resistor_SMD:R_0603_1608Metric -> Resistor_SMD:R_0402_1005Metric
- TP10, TP11, TP12, TP13, TP14, TP15, TP16, TP8, TP9: footprint TestPoint:TestPoint_Pad_D1.0mm -> TestPoint:TestPoint_Pad_D1.5mm; moved to F.Cu
- moved TP4 71.1 mm to (3.55, 121.1), turned to 0 degrees
- moved TP2 70.3 mm to (0.00, 121.1), turned to 0 degrees
- moved TP3 67.2 mm to (3.55, 117.5), turned to 0 degrees
- moved TP6 61.2 mm to (7.10, 121.1), turned to 0 degrees
- moved TP5 57.6 mm to (7.10, 117.5), turned to 0 degrees
- moved C27 42.0 mm to (58.9, 5.70)
- moved C28 42.0 mm to (52.3, 6.75)
- moved R29 42.0 mm to (52.9, 8.90)
- moved D2 42.0 mm to (52.1, 5.00)
- moved L2 42.0 mm to (56.0, 2.75)
- moved U9 42.0 mm to (56.0, 6.65)
- moved J6 27.0 mm to (62.9, 61.0)
- moved C2 17.0 mm to (56.0, 132.7)
- moved R1 17.0 mm to (60.4, 131.8)
- moved L1 17.0 mm to (58.1, 132.7)
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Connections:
- J2 pad A4: Net-(J2-VBUS_A) -> VUSB
- J2 pad A9: Net-(J2-VBUS_A) -> VUSB
- J2 pad B4: Net-(J2-VBUS_B) -> VUSB
- J2 pad B9: Net-(J2-VBUS_B) -> VUSB
- J8 pad 21: unconnected-(J8A-SW/CD-Pad21) -> uSD_SIM_CD
- J8 pad 22: unconnected-(J8A-S/GND-Pad22) -> GND
- J8 pad 23: unconnected-(J8A-GND-Pad23) -> GND
- R25 pad 1: uSD_DET -> uSD_SIM_CD
- TP2 pad 1: VUSB -> +3.3V
- TP3 pad 1: +3.3V -> VBAT
- TP4 pad 1: VBAT -> +1.8V
- TP5 pad 1: +1.8V -> GND
- TP6 pad 1: GND -> AGND
- U12 pad 3: GND -> +3.3V
- U8 pad 6: Net-(U8-DATA2_IN) -> SIM_DATA
- U8 pad 7: Net-(U8-CLK_IN) -> SIM_CLK
- U8 pad 8: Net-(U8-DATA1_IN) -> SIM_RST
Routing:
- net Net-(U3-BAT): track 0.00 -> 11.5 mm, vias 0 -> 2
- net VUSB: track 0.00 -> 2.57 mm
- net VBAT: track 0.00 -> 1.73 mm
- net SDA: track 0.00 -> 1.59 mm, vias 0 -> 1
- net Net-(U3-BIN): track 0.00 -> 1.36 mm
- net Net-(U2-PROG3): track 0.00 -> 1.28 mm
- net Net-(U3-VDD): track 0.00 -> 1.23 mm
- net Net-(U2-PROG1): track 0.00 -> 1.12 mm
- net SCL: track 0.00 -> 0.82 mm, vias 0 -> 1
- net FUEL_GPO: track 0.00 -> 0.73 mm, vias 0 -> 1
- added copper zone on B.Cu, net Net-(U3-BAT)
- added copper zone on B.Cu, net VBAT
- added copper zone on B.Cu, net VUSB
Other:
- board text removed: "Battery"

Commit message: Various Changes to footprints and components
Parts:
- removed the C29 at (57.8, 34.4)
- removed R26, R27, R28: 22R, Resistor_SMD:R_0402_1005Metric
- added TP7: TestPoint, TestPoint:TestPoint_Pad_D1.5mm, F.Cu at (16.3, 108.3)
- added U15: TPS22964CYZPR, TPS22964CYZPR:IC_SN74LVC2G34YZPR, B.Cu at (54.7, 133.2)
- C30: value 22pF -> 1uF; footprint Capacitor_SMD:C_0402_1005Metric -> Capacitor_SMD:C_0201_0603Metric; moved to B.Cu
- C31: value 22pF -> 100nF; footprint Capacitor_SMD:C_0402_1005Metric -> Capacitor_SMD:C_0201_0603Metric; moved to B.Cu
- FB1, FB2: value MPZ2012S221AT000 -> BLM18SG221TN1D; footprint MPZ2012S221AT000:BEADC2012X105N -> BLM18SG221TN1D:BEADC1608X65N
- L2: footprint WE-MAPI_3015:WE-MAPI_3015 -> custom_footprints:IND-SMD_L2.0-W1.2_MTQH201208S4R7MBT
- U12: moved to F.Cu
- U5, U7: value TXB0108RGYR -> TXB0108YZPR2; footprint TXB0108RGYR:IC_TXB0108RGYR -> TXB0108YZPR2:YZP20
- moved C30 100.3 mm to (56.8, 133.7)
- moved C31 99.2 mm to (56.1, 134.5)
- moved FB1 96.5 mm to (58.1, 45.1), turned to 90 degrees
- moved C38 94.6 mm to (56.1, 45.8)
- moved R32 94.6 mm to (56.1, 44.8)
- moved R33 94.6 mm to (56.1, 46.8)
- moved U13 94.6 mm to (53.3, 45.3)
- moved C42 94.5 mm to (52.7, 40.5)
- moved C45 94.4 mm to (56.1, 36.0)
- moved C47 94.4 mm to (57.1, 36.0)
- moved C39 94.4 mm to (60.4, 38.9)
- moved C40 94.4 mm to (60.4, 41.5)
- moved C43 94.4 mm to (60.4, 40.5)
- moved C44 94.4 mm to (60.4, 37.9)
- moved C46 94.4 mm to (52.3, 38.7)
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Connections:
- C27 pad 1: +3.3V -> +3.3V_SW
- C30 pad 1: SIM_RST -> +3.3V
- C31 pad 1: SIM_DATA -> +3.3V_SW
- FB1 pad 1: Net-(U14-VDDA) -> GND
- FB1 pad 2: +3.3V -> AGND
- FB2 pad 1: GND -> +3.3V
- FB2 pad 2: AGND -> Net-(U14-VDDA)
- L2 pad 1: +3.3V -> +3.3V_SW
- LED1 pad 2: +3.3V -> +3.3V_SW
- LED10 pad 2: +3.3V -> +3.3V_SW
- LED11 pad 2: +3.3V -> +3.3V_SW
- LED12 pad 2: +3.3V -> +3.3V_SW
- LED13 pad 2: +3.3V -> +3.3V_SW
- LED14 pad 2: +3.3V -> +3.3V_SW
- LED15 pad 2: +3.3V -> +3.3V_SW
- LED16 pad 2: +3.3V -> +3.3V_SW
- LED17 pad 2: +3.3V -> +3.3V_SW
- LED2 pad 2: +3.3V -> +3.3V_SW
- LED3 pad 2: +3.3V -> +3.3V_SW
- LED4 pad 2: +3.3V -> +3.3V_SW
- LED5 pad 2: +3.3V -> +3.3V_SW
- LED6 pad 2: +3.3V -> +3.3V_SW
- LED7 pad 2: +3.3V -> +3.3V_SW
- LED8 pad 2: +3.3V -> +3.3V_SW
- LED9 pad 2: +3.3V -> +3.3V_SW
- TP5 pad 1: GND -> +3.3V_SW
- TP6 pad 1: AGND -> GND
- U9 pad 5: +3.3V -> +3.3V_SW
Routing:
- net Net-(U3-BAT): track 11.5 -> 0.00 mm, vias 2 -> 0
- net VBAT: track 1.73 -> 0.00 mm
- net Net-(Q2-Pad1): track 0.00 -> 1.64 mm
- net SDA: track 1.59 -> 0.00 mm, vias 1 -> 0
- net Net-(U3-BIN): track 1.36 -> 0.00 mm
- net Net-(U2-PROG3): track 1.28 -> 0.00 mm
- net Net-(U3-VDD): track 1.23 -> 0.00 mm
- net Net-(U2-PROG1): track 1.12 -> 0.00 mm
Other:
- outline, holes or cut-outs redrawn
